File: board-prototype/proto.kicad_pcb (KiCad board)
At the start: 4 copper layers, 214.1 x 131.7 mm, 74 parts, among them P1 AB, P101 Data, P102 Power, P2 CD, U101 Am2908, U102 Am2908, U103 Am2908, U104 Am2908, U105 Am2908, U106 Am2908, U107 74LVC7T245, U108 74LVC7T245, U109 74LVC7T245, U110 MAX3488, U111 MAX3488, U112 MAX3488, U115 74LVC7T245, U116 74LVC7T245, U117 74LVC7T245, U118 74LVC7T245, U119 74LVC7T245, U120 LD1117S33CTR, U201 DS8641-LR, U202 DS8641-LR, U203 DS8641-LR, U204 DS8641-LR, U205 DS8641-LR

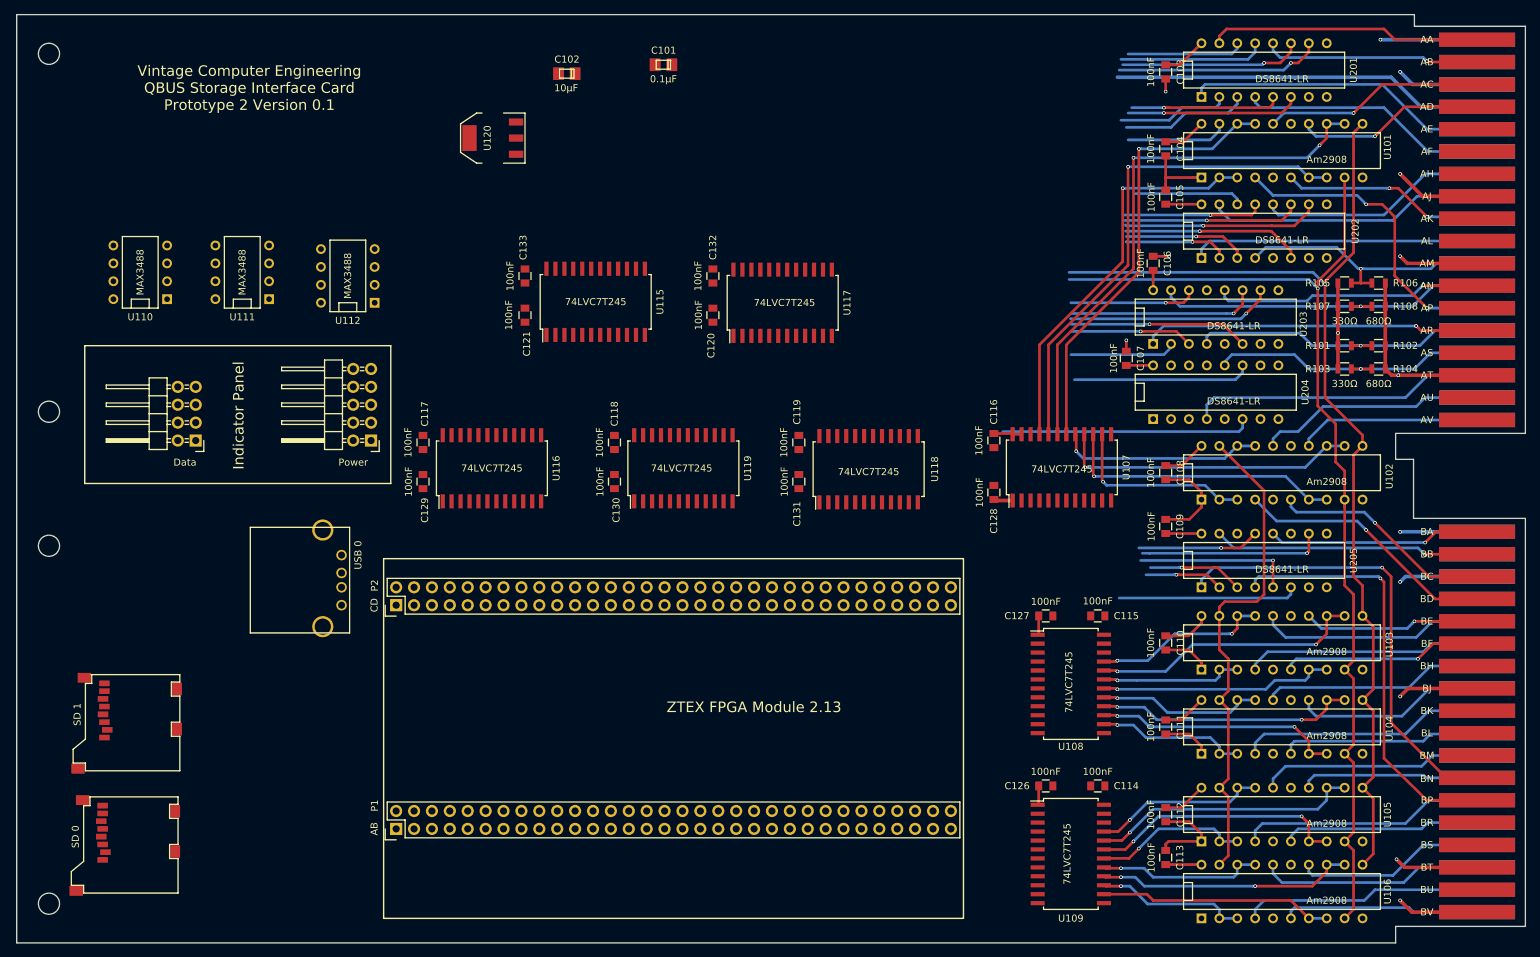
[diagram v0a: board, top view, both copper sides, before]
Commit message: Split schematic into multiple sheets.
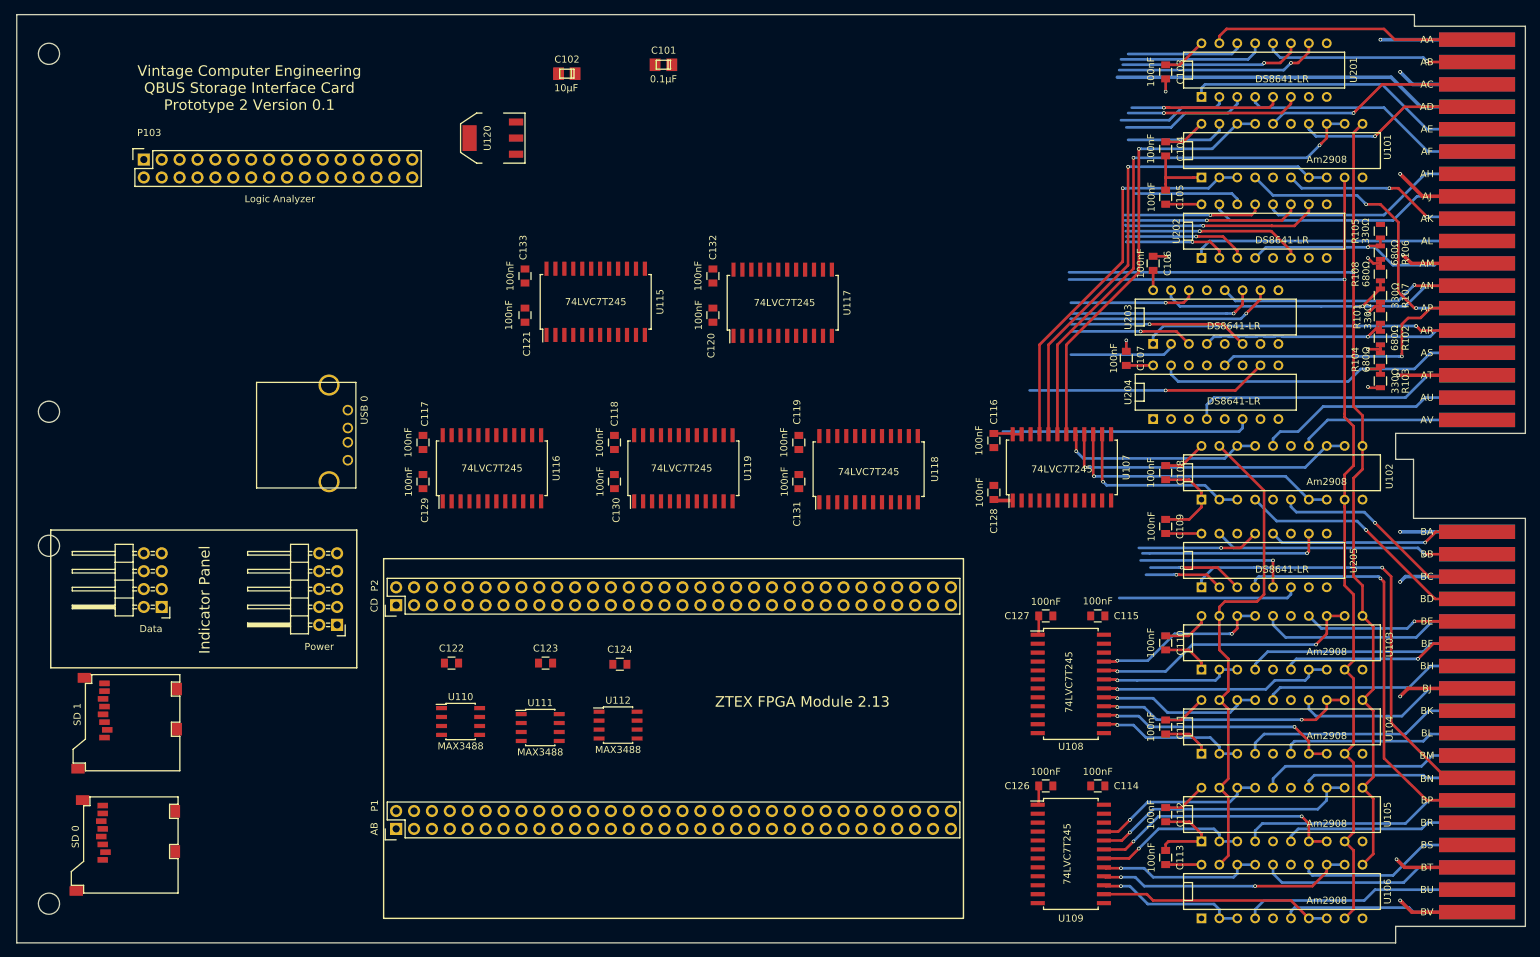
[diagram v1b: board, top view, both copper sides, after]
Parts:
- added C122: 100nF, Capacitors_SMD:C_0805, F.Cu at (94.0, 117.4)
- added C123: 100nF, Capacitors_SMD:C_0805, F.Cu at (107.3, 117.4)
- added C124: 100nF, Capacitors_SMD:C_0805, F.Cu at (117.9, 117.6)
- added P103: Logic Analyzer, Socket_Strips:Socket_Strip_Straight_2x16, F.Cu at (50.3, 46.0)
- U110, U111, U112: footprint Housings_DIP:DIP-8__300 -> Housings_SOIC:SOIC-8_3.9x4.9mm_Pitch1.27mm
- moved U110 78.3 mm to (95.2, 125.7), turned to 0 degrees
- moved U111 77.2 mm to (106.6, 126.6), turned to 0 degrees
- moved U112 74.4 mm to (117.6, 126.2), turned to 0 degrees
- moved P102 26.6 mm to (77.7, 112.0)
- moved P101 24.1 mm to (52.8, 109.5)
- moved USB 0 20.6 mm to (79.2, 81.5)
- moved R105 8.95 mm to (225.8, 56.1), turned to 270 degrees
- moved R101 6.55 mm to (225.8, 68.3), turned to 270 degrees
- moved R103 5.36 mm to (225.8, 77.4), turned to 90 degrees
- moved R107 5.30 mm to (225.8, 65.3), turned to 90 degrees
- moved R108 4.58 mm to (225.8, 62.2), turned to 90 degrees
- moved R106 4.33 mm to (225.8, 59.2), turned to 270 degrees
- moved R104 1.36 mm to (225.8, 74.4), turned to 90 degrees
- moved R102 1.11 mm to (225.8, 71.3), turned to 270 degrees
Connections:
- net /BBS7 renamed BBS7
- net /BDAL0 renamed BDAL0
- net /BDAL1 renamed BDAL1
- net /BDAL10 renamed BDAL10
- net /BDAL11 renamed BDAL11
- net /BDAL12 renamed BDAL12
- net /BDAL13 renamed BDAL13
- net /BDAL14 renamed BDAL14
- net /BDAL15 renamed BDAL15
- net /BDAL16 renamed BDAL16
- net /BDAL17 renamed BDAL17
- net /BDAL18 renamed BDAL18
- net /BDAL19 renamed BDAL19
- net /BDAL2 renamed BDAL2
- net /BDAL20 renamed BDAL20
- net /BDAL21 renamed BDAL21
- net /BDAL3 renamed BDAL3
- net /BDAL4 renamed BDAL4
- net /BDAL5 renamed BDAL5
- net /BDAL6 renamed BDAL6
- net /BDAL7 renamed BDAL7
- net /BDAL8 renamed BDAL8
- net /BDAL9 renamed BDAL9
- net /BDCOK renamed BDCOK
- net /BDIN renamed BDIN
- net /BDMGI renamed BDMGI
- net /BDMR renamed BDMR
- net /BDOUT renamed BDOUT
- net /BIAKI renamed BIAKI
- net /BIAKO renamed BIAKO
- net /BINIT renamed BINIT
- net /BIRQ4 renamed BIRQ4
- net /BIRQ5 renamed BIRQ5
- net /BIRQ6 renamed BIRQ6
- net /BIRQ7 renamed BIRQ7
- net /BPOK renamed BPOK
- net /BREF renamed BREF
- net /BRPLY renamed BRPLY
- net /BSACK renamed BSACK
- net /BSYNC renamed BSYNC
- net /BWTBT renamed BWTBT
- net /iDALst renamed DALst5
- net /iDALtx renamed DALtx5
- net /~iDALbe renamed ~DALbe5
- B101 pad AP1: Net-(B101-PadAP1) -> BHALT
- B101 pad AS2: /BDMGO -> BDMGO
- P2 pad 53: Net-(P2-Pad53) -> RHALT
- R103 pad 2: /BDMGO -> BDMGO
- R104 pad 1: /BDMGO -> BDMGO
- U118 pad 8: Net-(U118-Pad8) -> RHALT
- U204 pad 10: Net-(U204-Pad10) -> Net-(U118-Pad16)
- U204 pad 11: Net-(U117-Pad8) -> GND
- U204 pad 12: /BDMGO -> BHALT
- U204 pad 14: GND -> Net-(U117-Pad8)
- U204 pad 15: Net-(U204-Pad15) -> BDMGO
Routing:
- net BDMGO: track 0.00 -> 49.7 mm, vias 0 -> 1
- net BHALT: track 0.00 -> 42.4 mm, vias 0 -> 1
- net /BDMGO: track 41.5 -> 0.00 mm, vias 1 -> 0
- net Net-(U118-Pad16): track 0.00 -> 34.2 mm, vias 0 -> 1
- net Net-(U117-Pad8): track 25.8 -> 0.00 mm
- net GND: track 151.4 -> 143.4 mm, vias 10 -> 12
- net +5V: track 112.4 -> 105.3 mm, vias 4 -> 5
- net BIAKI: track 39.3 -> 36.3 mm
- net BIAKO: track 49.1 -> 50.9 mm
- net BDMGI: track 44.1 -> 42.8 mm
- net ~DALbe5: track 148.4 -> 149.5 mm
- net BBS7: track 44.1 -> 45.0 mm
- net BDMR: track 38.0 -> 37.4 mm

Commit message: Changed over to only DS8641 bus transceivers and the smaller package level-converters.
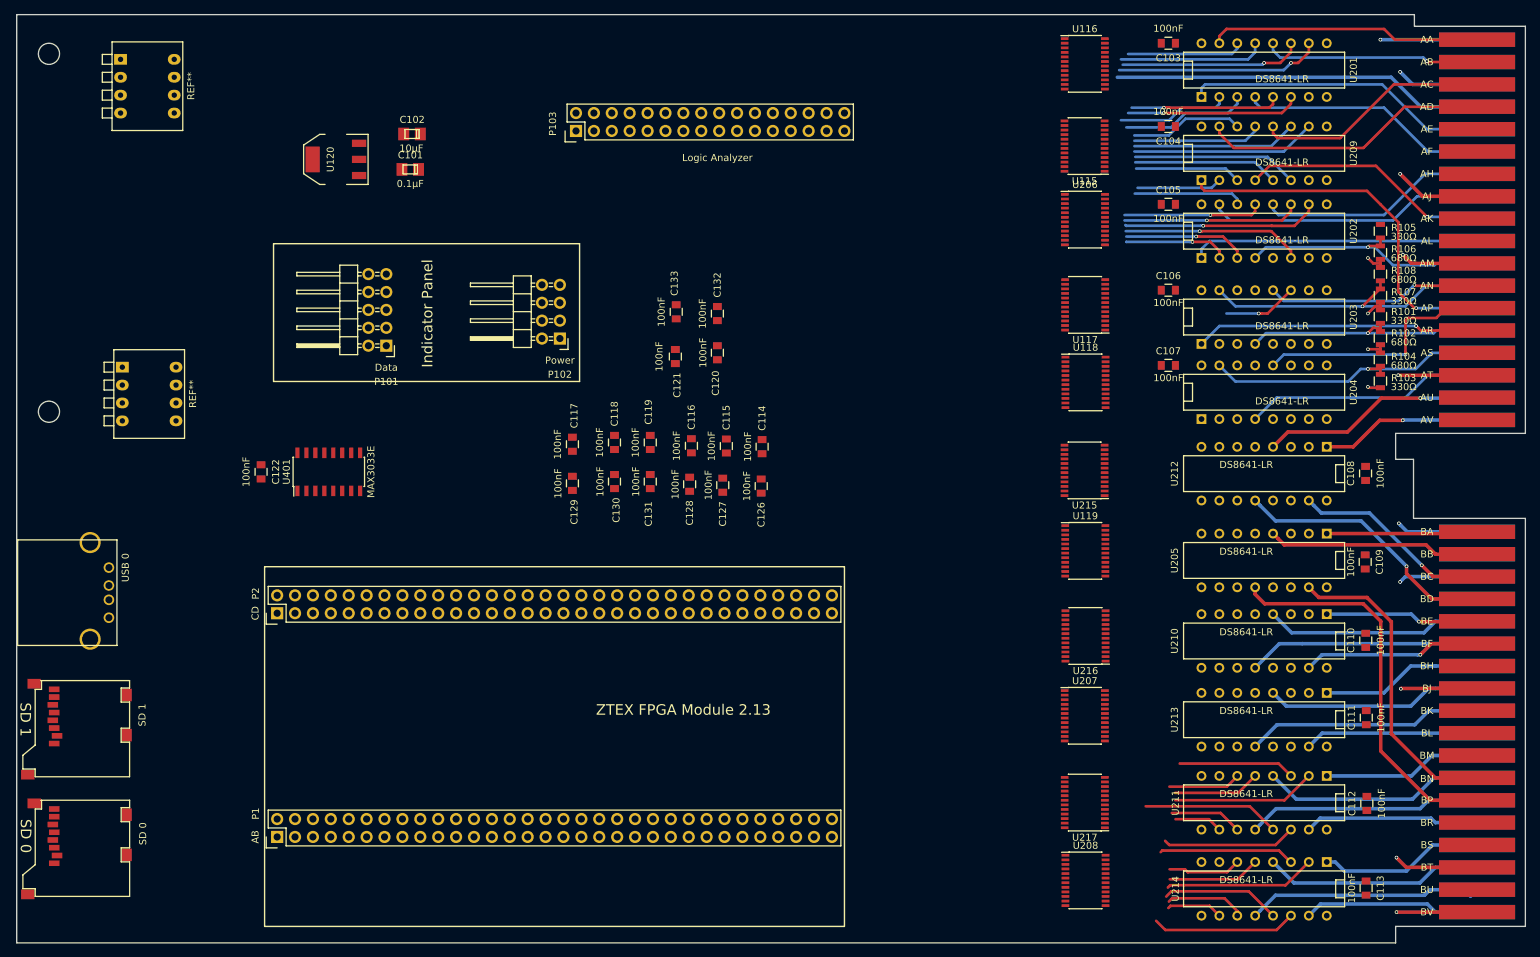
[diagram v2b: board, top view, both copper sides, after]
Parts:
- removed C123, C124: 100nF, Capacitors_SMD:C_0805
- removed the REF** at (32.3, 126.1)
- removed U101, U102, U103, U104, U105, U106: Am2908, Sockets_DIP:DIP-20__300
- removed U107, U108, U109: 74LVC7T245, Housings_SOIC:SOIC-24_7.5x15.4mm_Pitch1.27mm
- removed U110, U111, U112: MAX3488, Housings_SOIC:SOIC-8_3.9x4.9mm_Pitch1.27mm
- removed h3, h4: MountingHole_3mm, Mounting_Holes:MountingHole_3mm
- added REF**: SW_DIP_x4_Piano, Buttons_Switches_ThroughHole:SW_DIP_x4_Piano, F.Cu at (47.0, 31.8)
- added REF**: SW_DIP_x4_Piano, Buttons_Switches_ThroughHole:SW_DIP_x4_Piano, F.Cu at (47.2, 75.4)
- added U206: 74LVC8T245, Housings_SSOP:TSSOP-24_4.4x7.8mm_Pitch0.65mm, F.Cu at (183.9, 54.5)
- added U207: 74LVC8T245, Housings_SSOP:TSSOP-24_4.4x7.8mm_Pitch0.65mm, F.Cu at (183.9, 124.9)
- added U208: 74LVC8T245, Housings_SSOP:TSSOP-24_4.4x7.8mm_Pitch0.65mm, F.Cu at (183.9, 148.3)
- added U209: DS8641-LR, Sockets_DIP:DIP-16__300, F.Cu at (209.3, 45.1)
- added U210: DS8641-LR, Sockets_DIP:DIP-16__300, F.Cu at (209.3, 114.3)
- added U211: DS8641-LR, Sockets_DIP:DIP-16__300, F.Cu at (209.3, 137.3)
- added U212: DS8641-LR, Sockets_DIP:DIP-16__300, F.Cu at (209.3, 90.6)
- added U213: DS8641-LR, Sockets_DIP:DIP-16__300, F.Cu at (209.3, 125.5)
- added U214: DS8641-LR, Sockets_DIP:DIP-16__300, F.Cu at (209.3, 149.5)
- added U215: 74LVC8T245, Housings_SSOP:TSSOP-24_4.4x7.8mm_Pitch0.65mm, F.Cu at (183.8, 90.1)
- added U216: 74LVC8T245, Housings_SSOP:TSSOP-24_4.4x7.8mm_Pitch0.65mm, F.Cu at (183.9, 113.6)
- added U217: 74LVC8T245, Housings_SSOP:TSSOP-24_4.4x7.8mm_Pitch0.65mm, F.Cu at (183.8, 137.2)
- added U401: MAX3033E, Housings_SOIC:SOIC-16_3.9x9.9mm_Pitch1.27mm, F.Cu at (76.5, 90.3)
- B101: footprint Qbus-double -> myMods.pretty:Qbus-double
- P101: footprint Pin_Headers:Pin_Header_Angled_2x04 -> Pin_Headers:Pin_Header_Angled_2x05
- P102: footprint Pin_Headers:Pin_Header_Angled_2x05 -> Pin_Headers:Pin_Header_Angled_2x04
- P103: footprint Socket_Strips:Socket_Strip_Straight_2x16 -> Pin_Headers:Pin_Header_Straight_2x16
- REF**: footprint DEC-Handle -> myMods.pretty:DEC-Handle
- SD 0: footprint myMods.pretty:microSD-3M-2900-series -> microSD-3M-2900-series
- U115, U116, U117, U118, U119: value 74LVC7T245 -> 74LVC8T245; footprint Housings_SOIC:SOIC-24_7.5x15.4mm_Pitch1.27mm -> Housings_SSOP:TSSOP-24_4.4x7.8mm_Pitch0.65mm
- moved U116 101.9 mm to (183.8, 32.4), turned to 0 degrees
- moved U115 72.8 mm to (183.8, 44.1), turned to 180 degrees
- moved C114 67.7 mm to (138.0, 86.7), turned to 270 degrees
- moved P103 61.5 mm to (111.6, 41.9), turned to 90 degrees
- moved C126 58.7 mm to (137.9, 92.3), turned to 90 degrees
- moved U119 58.2 mm to (183.9, 101.5), turned to 0 degrees
- moved C115 58.0 mm to (133.0, 86.6), turned to 270 degrees
- moved P102 51.5 mm to (109.3, 71.4)
- moved C127 49.5 mm to (132.5, 92.2), turned to 90 degrees
- moved P101 48.9 mm to (84.7, 72.4)
- moved C128 43.2 mm to (127.8, 92.1)
- moved C116 42.9 mm to (128.0, 86.6)
- moved U117 42.9 mm to (183.9, 66.6), turned to 180 degrees
- moved USB 0 40.6 mm to (45.3, 103.9)
- moved C101 38.9 mm to (88.1, 47.4)
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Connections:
- P1 pad 10: ZDAL0 -> TDAL2
- P1 pad 11: Net-(P1-Pad11) -> RDAL3
- P1 pad 12: ZDAL1 -> TDAL3
- P1 pad 13: ZDAL2 -> RDAL4
- P1 pad 14: ZDAL3 -> TDAL4
- P1 pad 15: ZDAL4 -> RDAL5
- P1 pad 16: ZDAL5 -> TDAL5
- P1 pad 17: ZDAL6 -> RDAL6
- P1 pad 18: Net-(P1-Pad18) -> TDAL6
- P1 pad 19: ZDAL7 -> RDAL7
- P1 pad 20: Net-(P1-Pad20) -> TDAL7
- P1 pad 21: ZDAL8 -> RDAL8
- P1 pad 22: Net-(P1-Pad22) -> TDAL8
- P1 pad 23: ZDAL9 -> RDAL9
- P1 pad 25: ZDAL10 -> RDAL10
- P1 pad 26: ZDAL11 -> TDAL9
- P1 pad 27: ZDAL12 -> RDAL11
- P1 pad 28: ZDAL13 -> TDAL10
- P1 pad 35: ZDAL14 -> RDAL12
- P1 pad 36: ZDAL15 -> TDAL11
- P1 pad 37: Net-(P1-Pad37) -> RDAL13
- P1 pad 38: Net-(P1-Pad38) -> TDAL12
- P1 pad 39: ZDAL16 -> RDAL14
- P1 pad 40: ZDAL17 -> TDAL13
- P1 pad 41: ZDAL18 -> RDAL15
- P1 pad 42: ZDAL19 -> TDAL14
- P1 pad 43: Net-(P1-Pad43) -> RDAL16
- P1 pad 44: Net-(P1-Pad44) -> TDAL15
- P1 pad 45: ZDAL20 -> RDAL17
- P1 pad 46: ZDAL21 -> TDAL16
- P1 pad 47: ZBS7 -> RDAL18
- P1 pad 48: ZWTBT -> TDAL17
- P1 pad 5: Net-(P1-Pad5) -> RDAL0
- P1 pad 50: Net-(P1-Pad50) -> TDAL18
- P1 pad 51: DALtx -> RDAL19
- P1 pad 52: Net-(P1-Pad52) -> TDAL19
- P1 pad 53: DALst -> RDAL20
- P1 pad 54: Net-(P1-Pad54) -> TDAL20
- P1 pad 55: ~DALbe -> RDAL21
- P1 pad 56: Net-(P1-Pad56) -> TDAL21
- P1 pad 57: Net-(P1-Pad57) -> RBS7
- P1 pad 58: Net-(P1-Pad58) -> TBS7
- P1 pad 59: Net-(P1-Pad59) -> RWTBT
- P1 pad 6: Net-(P1-Pad6) -> TDAL0
- P1 pad 60: Net-(P1-Pad60) -> TWTBT
- P1 pad 7: Net-(P1-Pad7) -> RDAL1
- P1 pad 8: Net-(P1-Pad8) -> TDAL1
- P1 pad 9: Net-(P1-Pad9) -> RDAL2
- P101 pad 1: IPdataP -> IPlatch_P
- P101 pad 2: IPdataN -> IPlatch_N
- P101 pad 3: IPclkP -> IPdata_P
- P101 pad 4: Net-(P101-Pad4) -> IPdata_N
- P101 pad 6: IPclkN -> Net-(P101-Pad6)
- P101 pad 7: IPlatchP -> IPclk_P
- P101 pad 8: IPlatchN -> IPclk_N
- P102 pad 1: +12V -> GND
- P102 pad 2: +12V -> GND
- P102 pad 3: GND -> +12V
- P102 pad 4: GND -> +12V
- P102 pad 5: GND -> +12V
- P102 pad 6: GND -> +12V
- U117 pad 10: ~DALbe5 -> Net-(U117-Pad10)
- U117 pad 14: ~DALbe -> Net-(U117-Pad14)
- U117 pad 15: DALst -> Net-(U117-Pad15)
- U117 pad 18: DALtx -> Net-(U117-Pad18)
- U117 pad 6: DALtx5 -> Net-(U117-Pad6)
- U117 pad 9: DALst5 -> Net-(U117-Pad9)
- U205 pad 1: BSACK -> BDCOK
- U205 pad 12: BDCOK -> BIRQ7
- U205 pad 15: BPOK -> BSACK
- U205 pad 4: BIRQ7 -> BPOK
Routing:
- net DALtx5: track 151.4 -> 0.00 mm, vias 1 -> 0
- net ~DALbe5: track 149.5 -> 0.00 mm, vias 1 -> 0
- net DALst5: track 85.0 -> 0.00 mm
- net Net-(U101-Pad12): track 76.9 -> 0.00 mm, vias 2 -> 0
- net Net-(U101-Pad7): track 71.7 -> 0.00 mm, vias 1 -> 0
- net +5V: track 105.3 -> 41.9 mm
- net Net-(U101-Pad17): track 62.8 -> 0.00 mm, vias 1 -> 0
- net GND: track 143.4 -> 86.4 mm, vias 12 -> 9
- net Net-(U101-Pad2): track 56.9 -> 0.00 mm, vias 1 -> 0
- net Net-(U102-Pad12): track 43.0 -> 0.00 mm, vias 1 -> 0
- net Net-(U102-Pad7): track 40.6 -> 0.00 mm, vias 1 -> 0
- net Net-(U103-Pad12): track 38.8 -> 0.00 mm, vias 2 -> 0
- net Net-(U105-Pad12): track 38.2 -> 0.00 mm, vias 1 -> 0
- net Net-(U104-Pad12): track 36.7 -> 0.00 mm, vias 2 -> 0
- net Net-(U106-Pad12): track 36.5 -> 0.00 mm, vias 2 -> 0
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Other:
- board text added: "SD 0"
- board text added: "SD 1"
- board text removed: "Vintage Computer Engineering QBUS Storage Interface Card Prototype 2 Version 0.1"
